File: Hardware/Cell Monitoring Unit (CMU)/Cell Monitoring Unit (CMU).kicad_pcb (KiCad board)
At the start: 4 copper layers, 144.7 x 95.9 mm, 186 parts, among them J1 705550056, J10 NTC-6, J11 NTC-7, J12 NTC-8, J2 JUMPER, J3 HIGH SIDE, J4 LOW SIDE, J5 NTC-1, J6 NTC-2, J7 NTC-3, J8 NTC-4, J9 NTC-5, T1 CEP99-102, T2 CEP99-102, U1 ZXTN4004KQTC, U2 PBQ79616PAPTQ1, U3 PESD5V0L2BT, U4 PESD5V0L2BT

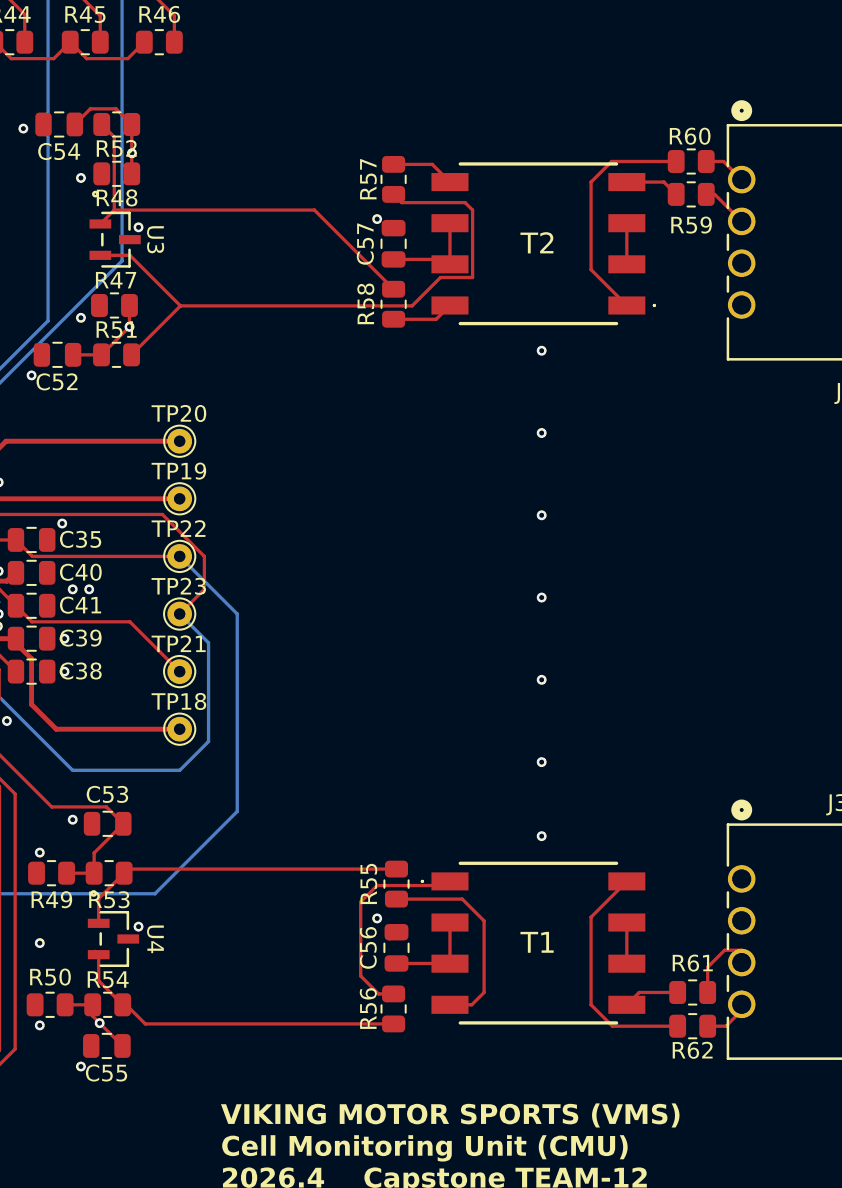
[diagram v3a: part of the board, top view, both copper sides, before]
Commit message: change iso+update cmu BOM
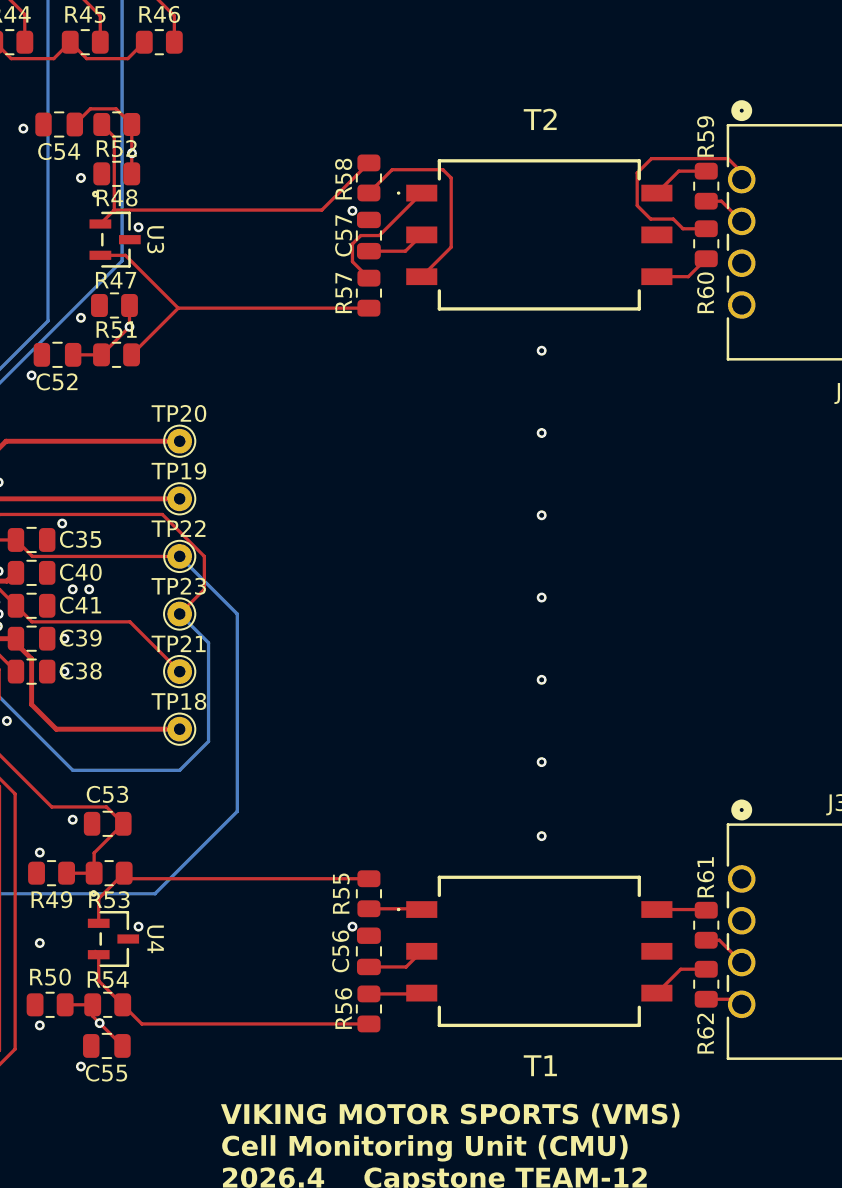
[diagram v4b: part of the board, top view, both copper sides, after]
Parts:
- T1, T2: value CEP99-102 -> HM2147NLT; footprint Footprints:CEP99102 -> Footprints:HM2147NLT
- moved R58 7.82 mm to (179.5, 74.0)
- moved R57 7.07 mm to (179.5, 81.0)
- moved R60 5.08 mm to (200.0, 78.0), turned to -90 degrees
- moved R61 4.17 mm to (200.0, 119.4), turned to 90 degrees
- moved R62 2.68 mm to (200.0, 123.0), turned to 90 degrees
- moved R55 1.78 mm to (179.5, 117.5)
- moved C56 1.69 mm to (179.5, 121.0)
- moved C57 1.58 mm to (179.5, 77.5)
- moved R56 1.50 mm to (179.5, 124.5)
- moved R59 1.04 mm to (200.0, 74.5), turned to 90 degrees
- moved T2 0.54 mm to (189.9, 77.5), turned to -90 degrees
- moved T1 0.50 mm to (189.9, 121.0), turned to -90 degrees
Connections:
- C56 pad 1: Net-(C56-Pad1) -> Net-(T1-PRI_2)
- C57 pad 1: Net-(C57-Pad1) -> Net-(T2-PRI_2)
- R55 pad 1: Net-(R55-Pad1) -> Net-(T1-PRI_1)
- R56 pad 1: Net-(R56-Pad1) -> Net-(T1-PRI_3)
- R57 pad 1: Net-(R57-Pad1) -> Net-(T2-PRI_1)
- R58 pad 1: Net-(R58-Pad1) -> Net-(T2-PRI_3)
- R59 pad 2: Net-(R59-Pad2) -> Net-(T2-SEC_3)
- R60 pad 2: Net-(R60-Pad2) -> Net-(T2-SEC_1)
- R61 pad 2: Net-(R61-Pad2) -> Net-(T1-SEC_3)
- R62 pad 2: Net-(R62-Pad2) -> Net-(T1-SEC_1)
- T1 pad 1: Net-(R56-Pad1) -> Net-(T1-PRI_1)
- T1 pad 2: Net-(C56-Pad1) -> Net-(T1-PRI_2)
- T1 pad 3: Net-(C56-Pad1) -> Net-(T1-PRI_3)
- T1 pad 4: Net-(R55-Pad1) -> Net-(T1-SEC_1)
- T1 pad 5: Net-(R61-Pad2) -> unconnected-(T1-SEC_2-Pad5)
- T1 pad 6: Net-(T1-Pad6) -> Net-(T1-SEC_3)
- T2 pad 1: Net-(R60-Pad2) -> Net-(T2-PRI_1)
- T2 pad 2: Net-(T2-Pad2) -> Net-(T2-PRI_2)
- T2 pad 3: Net-(T2-Pad2) -> Net-(T2-PRI_3)
- T2 pad 4: Net-(R59-Pad2) -> Net-(T2-SEC_1)
- T2 pad 5: Net-(R57-Pad1) -> unconnected-(T2-SEC_2-Pad5)
- T2 pad 6: Net-(C57-Pad1) -> Net-(T2-SEC_3)
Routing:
- net /CMU-Daisy-Chain Interface/COMLP_OPT: track 38.1 -> 21.7 mm
- net Net-(R62-Pad2): track 14.2 -> 0.00 mm
- net Net-(R60-Pad2): track 14.1 -> 0.00 mm
- net Net-(R56-Pad1): track 12.9 -> 0.00 mm
- net Net-(R55-Pad1): track 12.6 -> 0.00 mm
- net Net-(T2-PRI_3): track 0.00 -> 12.5 mm
- net /CMU-Daisy-Chain Interface/ISO_COMLN: track 2.61 -> 14.3 mm
- net Net-(T2-PRI_1): track 0.00 -> 7.98 mm
- net Net-(C57-Pad1): track 6.05 -> 0.00 mm
- net Net-(C56-Pad1): track 5.76 -> 0.00 mm
- net Net-(R57-Pad1): track 3.87 -> 0.00 mm
- net Net-(R58-Pad1): track 3.77 -> 0.00 mm
- net Net-(T2-PRI_2): track 0.00 -> 3.62 mm
- net Net-(T1-PRI_2): track 0.00 -> 3.60 mm
- net Net-(T1-SEC_1): track 0.00 -> 3.60 mm
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
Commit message: finish! update bmu layout+BOM
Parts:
- C38: value 1uF -> 1u
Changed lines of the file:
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@@
 			)
 		)
-		(property "MPN" "8.85382E+11"
+		(property "MPN" "885382207008"
 			(at 0 0 0)
 			(unlocked yes)
@@
 			)
 		)
-		(property "MPN" "8.85012E+11"
+		(property "MPN" "885012207079"
 			(at 0 0 90)
 			(unlocked yes)
@@
 			)
 		)
-		(property "Value" "1uF"
+		(property "Value" "1u"
 			(at 0 1.68 0)
 			(layer "F.Fab")
